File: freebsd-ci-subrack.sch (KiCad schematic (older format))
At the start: 1 part

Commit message: Add main parts
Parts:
- added C?: 100n, symbol Device:C
- added C?: 10n, symbol Device:C
- added D?: RX, symbol Device:LED
- added D?: TX, symbol Device:LED
- added D?: TGT_PWR, symbol Device:LED
- added Q?: Q_PMOS_GDS, symbol Device:Q_PMOS_GDS
- added Q?: 2N7002, Package_TO_SOT_SMD:SOT-23, symbol Transistor_FET:2N7002
- added R?: R, symbol Device:R
- added R? (x5): 5K, symbol Device:R
- added R?: 100K, symbol Device:R
- added R? (x2): 10K, symbol Device:R
- added TP?: SDA, symbol Connector:TestPoint
- added TP?: SCL, symbol Connector:TestPoint
- added U?: MCP2221A, symbol Subrack:MCP2221A
- added U?: INA219BxD, Package_SO:SOIC-8_3.9x4.9mm_P1.27mm, symbol Analog_ADC:INA219BxD
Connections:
- net labels added: +3V3, +5V_SW, +5V_TGT, PWRON, SCL, SDA
- wire segments 17 -> 81
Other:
- note added: "Backplane Connector"
- note added: "USB Interface"
- moved on the sheet: J?

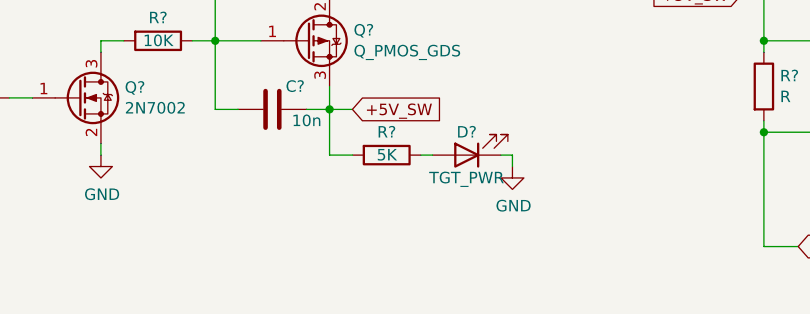
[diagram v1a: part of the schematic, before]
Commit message: Add reference to ON Semi load switch app note
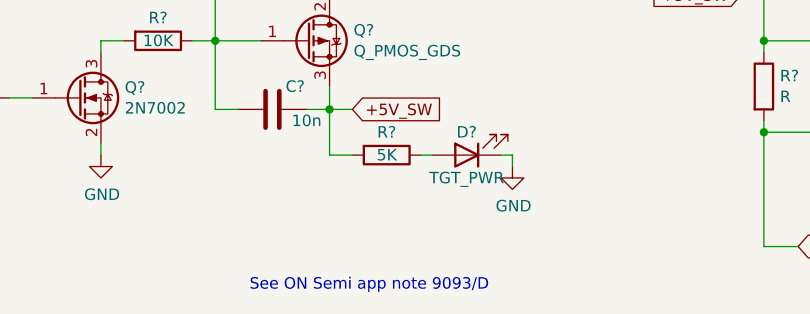
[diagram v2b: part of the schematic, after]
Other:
- note added: "See ON Semi app note 9093/D"
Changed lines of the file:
@@
 	4850 5800 5000 5800
 Connection ~ 4850 5300
+Text Notes 2600 6000 0    50   ~ 0
+See ON Semi app note 9093/D
 $EndSCHEMATC

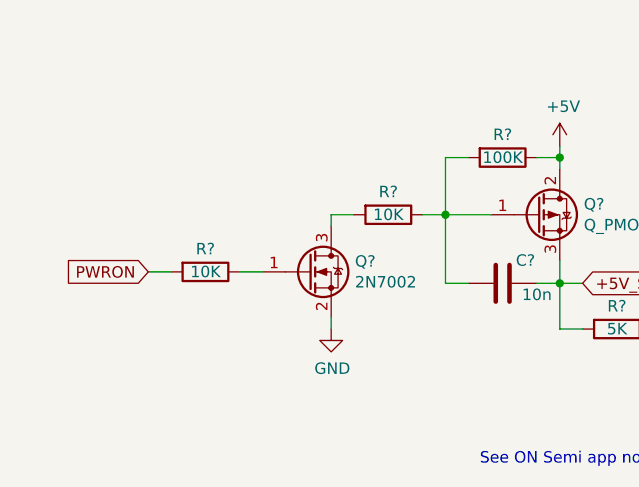
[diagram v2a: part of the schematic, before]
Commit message: Use an inverter instead of 2N7002
Allow us to drive the gate high, turning the PFET off more
quickly.
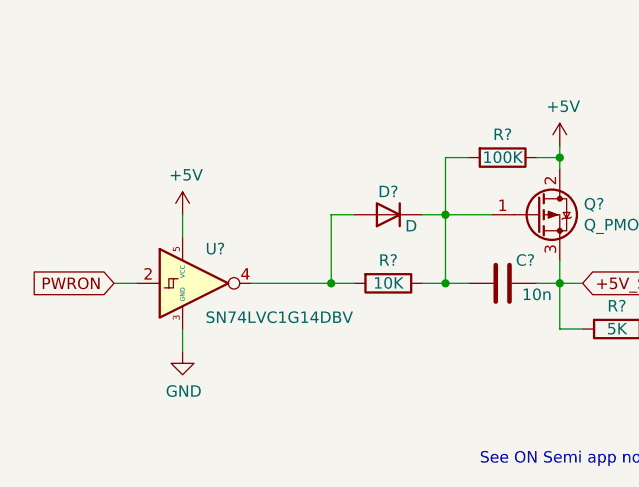
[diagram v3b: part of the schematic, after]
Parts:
- removed Q?: 2N7002, Package_TO_SOT_SMD:SOT-23, symbol Transistor_FET:2N7002
- removed R?: 10K, symbol Device:R
- added D?: D, symbol Device:D
- added U?: SN74LVC1G14DBV, Package_TO_SOT_SMD:SOT-23-5, symbol 74xGxx:SN74LVC1G14DBV
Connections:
- wire segments 81 -> 84
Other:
- moved on the sheet: R?
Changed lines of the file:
@@
 	2950 4600 2950 4650
-$Comp
-L Transistor_FET:2N7002 Q?
-U 1 1 609C94BD
-P 1850 5150
-F 0 "Q?" H 2054 5196 50  0000 L CNN
-F 1 "2N7002" H 2054 5105 50  0000 L CNN
-F 2 "Package_TO_SOT_SMD:SOT-23" H 2050 5075 50  0001 L CIN
-F 3 "https://www.onsemi.com/pub/Collateral/NDS7002A-D.PDF" H 1850 5150 50  0001 L CNN
-	1    1850 5150
-	1    0    0    -1
-$EndComp
-$Comp
-L power:GND #PWR?
-U 1 1 609CBBCB
-P 1950 5400
-F 0 "#PWR?" H 1950 5150 50  0001 C CNN
-F 1 "GND" H 1955 5227 50  0000 C CNN
-F 2 "" H 1950 5400 50  0001 C CNN
-F 3 "" H 1950 5400 50  0001 C CNN
-	1    1950 5400
-	1    0    0    -1
-$EndComp
 $Comp
 L Device:C C?
@@
 L Device:R R?
 U 1 1 609D742E
-P 2200 4900
-F 0 "R?" V 2100 4900 50  0000 C CNN
-F 1 "10K" V 2200 4900 50  0000 C CNN
-F 2 "" V 2130 4900 50  0001 C CNN
-F 3 "~" H 2200 4900 50  0001 C CNN
-	1    2200 4900
-	0    1    1    0
-$EndComp
-Wire Wire Line
-	2050 4900 1950 4900
-Wire Wire Line
-	1950 4900 1950 4950
-Wire Wire Line
-	1950 5350 1950 5400
+P 2200 5200
+F 0 "R?" V 2100 5200 50  0000 C CNN
+F 1 "10K" V 2200 5200 50  0000 C CNN
+F 2 "" V 2130 5200 50  0001 C CNN
+F 3 "~" H 2200 5200 50  0001 C CNN
+	1    2200 5200
+	0    1    1    0
+$EndComp
 $Comp
 L Device:LED D?
@@
 	9250 1050 9250 1150
 Connection ~ 9250 1150
-Text GLabel 1150 5150 0    50   Input ~ 0
+Text GLabel 1000 5200 0    50   Input ~ 0
 PWRON
-$Comp
-L Device:R R?
-U 1 1 60A711D5
-P 1400 5150
-F 0 "R?" V 1300 5150 50  0000 C CNN
-F 1 "10K" V 1400 5150 50  0000 C CNN
-F 2 "" V 1330 5150 50  0001 C CNN
-F 3 "~" H 1400 5150 50  0001 C CNN
-	1    1400 5150
-	0    1    1    0
-$EndComp
-Wire Wire Line
-	1550 5150 1650 5150
-Wire Wire Line
-	1150 5150 1250 5150
 Text GLabel 4750 4700 0    50   Input ~ 0
 +5V_SW
@@
 Text Notes 2600 6000 0    50   ~ 0
 See ON Semi app note 9093/D
+$Comp
+L 74xGxx:SN74LVC1G14DBV U?
+U 1 1 60A853C9
+P 1300 5200
+F 0 "U?" H 1400 5350 50  0000 L CNN
+F 1 "SN74LVC1G14DBV" H 1400 5050 50  0000 L CNN
+F 2 "Package_TO_SOT_SMD:SOT-23-5" H 1300 4950 50  0001 C CNN
+F 3 "http://www.ti.com/lit/ds/symlink/sn74lvc1g14.pdf" H 1300 5200 50  0001 C CNN
+	1    1300 5200
+	1    0    0    -1
+$EndComp
+Wire Wire Line
+	1000 5200 1100 5200
+$Comp
+L Device:D D?
+U 1 1 60A911C4
+P 2200 4900
+F 0 "D?" H 2200 4800 50  0000 C CNN
+F 1 "D" H 2100 4950 50  0000 C CNN
+F 2 "" H 2200 4900 50  0001 C CNN
+F 3 "~" H 2200 4900 50  0001 C CNN
+	1    2200 4900
+	-1   0    0    1
+$EndComp
+Wire Wire Line
+	2350 5200 2450 5200
+Connection ~ 2450 5200
+Wire Wire Line
+	2050 5200 1950 5200
+Wire Wire Line
+	1950 5200 1950 4900
+Wire Wire Line
+	1950 4900 2050 4900
+Wire Wire Line
+	1600 5200 1950 5200
+Connection ~ 1950 5200
+$Comp
+L power:+5V #PWR?
+U 1 1 60AA2B40
+P 1300 4900
+F 0 "#PWR?" H 1300 4750 50  0001 C CNN
+F 1 "+5V" H 1315 5073 50  0000 C CNN
+F 2 "" H 1300 4900 50  0001 C CNN
+F 3 "" H 1300 4900 50  0001 C CNN
+	1    1300 4900
+	1    0    0    -1
+$EndComp
+Wire Wire Line
+	1300 5000 1300 4900
+$Comp
+L power:GND #PWR?
+U 1 1 60AA5425
+P 1300 5500
+F 0 "#PWR?" H 1300 5250 50  0001 C CNN
+F 1 "GND" H 1305 5327 50  0000 C CNN
+F 2 "" H 1300 5500 50  0001 C CNN
+F 3 "" H 1300 5500 50  0001 C CNN
+	1    1300 5500
+	1    0    0    -1
+$EndComp
+Wire Wire Line
+	1300 5500 1300 5400
 $EndSCHEMATC

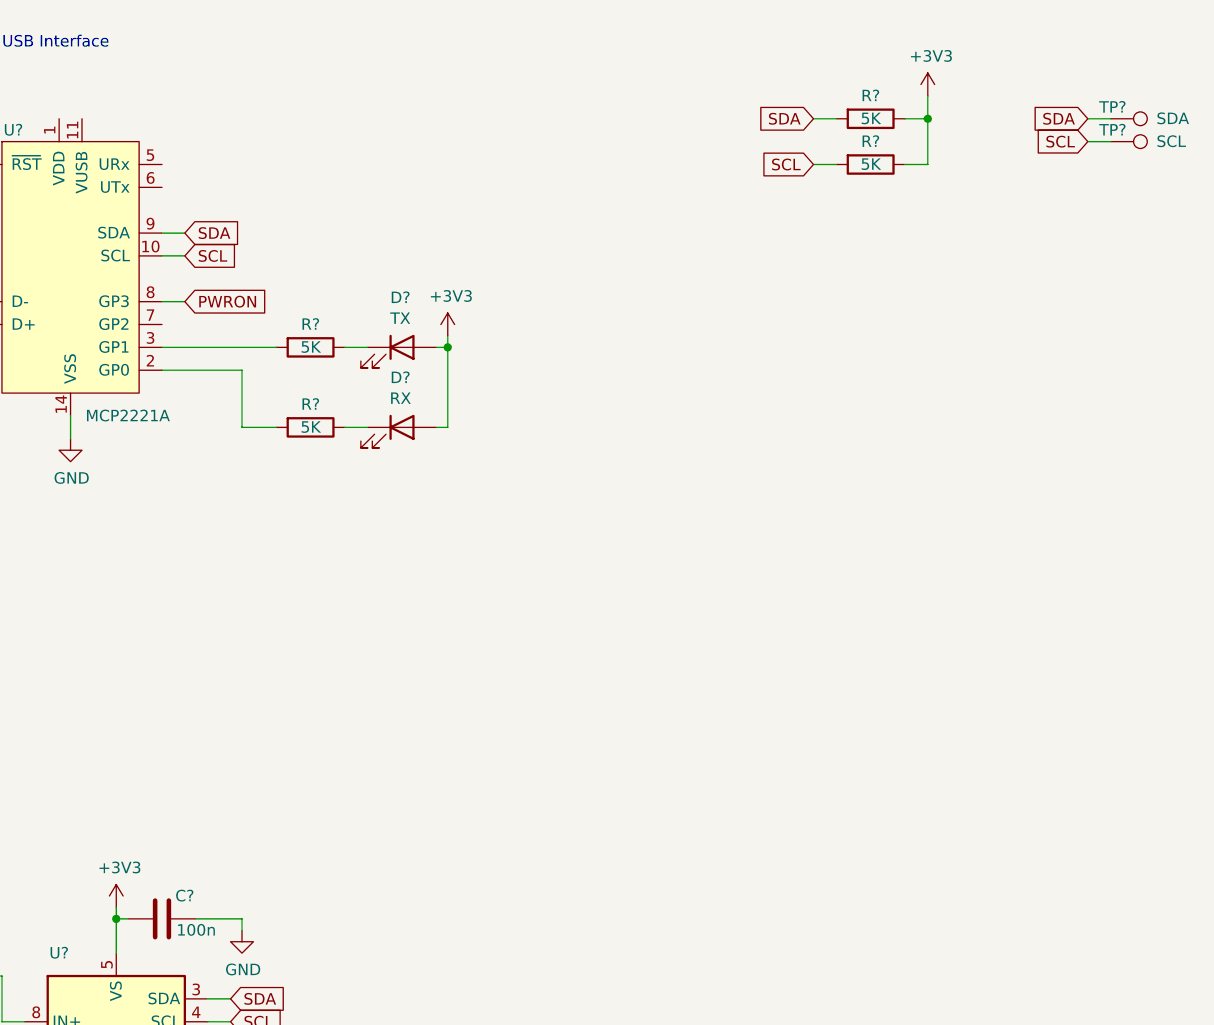
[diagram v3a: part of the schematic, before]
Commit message: Add a buffer for TX to target
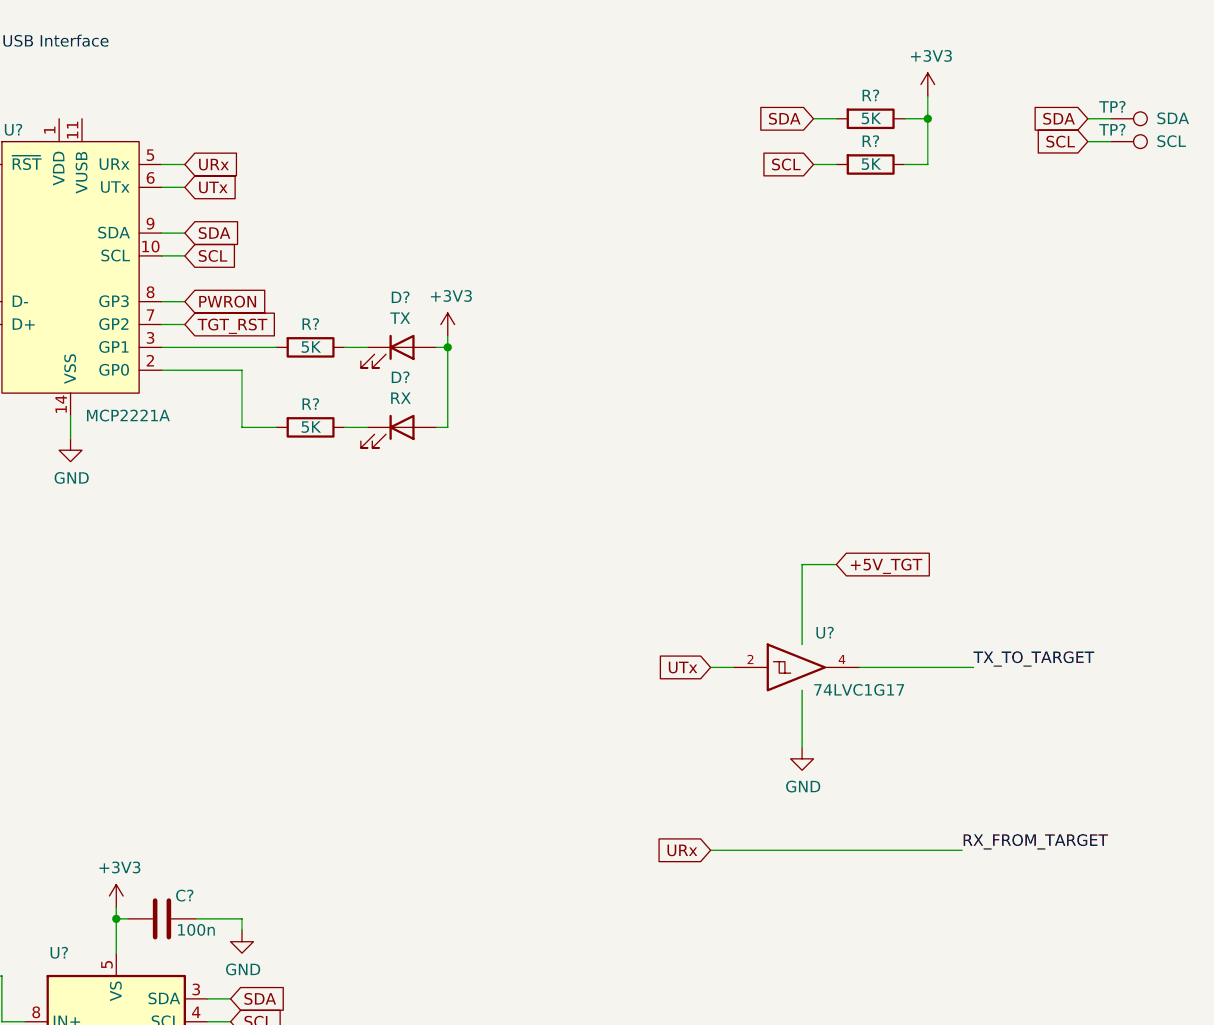
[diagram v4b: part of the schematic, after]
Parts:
- added U?: 74LVC1G17, symbol 74xGxx:74LVC1G17
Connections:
- net labels added: RX_FROM_TARGET, TGT_RST, TX_TO_TARGET, URx, UTx
- wire segments 84 -> 93
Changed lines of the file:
@@
 Wire Wire Line
 	1300 5500 1300 5400
+$Comp
+L 74xGxx:74LVC1G17 U?
+U 1 1 60AADB57
+P 8700 3550
+F 0 "U?" H 8800 3700 50  0000 C CNN
+F 1 "74LVC1G17" H 8950 3450 50  0000 C CNN
+F 2 "" H 8700 3550 50  0001 C CNN
+F 3 "http://www.ti.com/lit/sg/scyt129e/scyt129e.pdf" H 8700 3550 50  0001 C CNN
+	1    8700 3550
+	1    0    0    -1
+$EndComp
+Text GLabel 8850 3100 2    50   Input ~ 0
++5V_TGT
+Wire Wire Line
+	8700 3450 8700 3100
+Wire Wire Line
+	8700 3100 8850 3100
+$Comp
+L power:GND #PWR?
+U 1 1 60AB1679
+P 8700 3900
+F 0 "#PWR?" H 8700 3650 50  0001 C CNN
+F 1 "GND" H 8705 3727 50  0000 C CNN
+F 2 "" H 8700 3900 50  0001 C CNN
+F 3 "" H 8700 3900 50  0001 C CNN
+	1    8700 3900
+	1    0    0    -1
+$EndComp
+Wire Wire Line
+	8700 3650 8700 3900
+Text GLabel 6000 1350 2    50   Input ~ 0
+URx
+Text GLabel 6000 1450 2    50   Input ~ 0
+UTx
+Wire Wire Line
+	5900 1450 6000 1450
+Wire Wire Line
+	5900 1350 6000 1350
+Text GLabel 8300 3550 0    50   Input ~ 0
+UTx
+Wire Wire Line
+	8300 3550 8400 3550
+Text Label 9450 3550 0    50   ~ 0
+TX_TO_TARGET
+Wire Wire Line
+	8950 3550 9450 3550
+Text GLabel 8300 4350 0    50   Input ~ 0
+URx
+Text Label 9400 4350 0    50   ~ 0
+RX_FROM_TARGET
+Wire Wire Line
+	8300 4350 9400 4350
+Text GLabel 6000 2050 2    50   Input ~ 0
+TGT_RST
+Wire Wire Line
+	5900 2050 6000 2050
 $EndSCHEMATC

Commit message: Change 12V to NC - we're not using it on this board
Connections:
- net labels removed: +12V
- wire segments 93 -> 89
- no-connect marks 0 -> 2
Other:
- note added: "12V"
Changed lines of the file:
@@
 $EndComp
-$Comp
-L power:+12V #PWR?
-U 1 1 60985629
-P 1300 1350
-F 0 "#PWR?" H 1300 1200 50  0001 C CNN
-F 1 "+12V" H 1315 1523 50  0000 C CNN
-F 2 "" H 1300 1350 50  0001 C CNN
-F 3 "" H 1300 1350 50  0001 C CNN
-	1    1300 1350
-	1    0    0    -1
-$EndComp
-Wire Wire Line
-	1350 1400 1300 1400
-Wire Wire Line
-	1300 1400 1300 1350
-$Comp
-L power:+12V #PWR?
-U 1 1 60986720
-P 1900 1350
-F 0 "#PWR?" H 1900 1200 50  0001 C CNN
-F 1 "+12V" H 1915 1523 50  0000 C CNN
-F 2 "" H 1900 1350 50  0001 C CNN
-F 3 "" H 1900 1350 50  0001 C CNN
-	1    1900 1350
-	1    0    0    -1
-$EndComp
-Wire Wire Line
-	1850 1400 1900 1400
-Wire Wire Line
-	1900 1400 1900 1350
 $Comp
 L power:+5V #PWR?
@@
 Wire Wire Line
 	5900 2050 6000 2050
+NoConn ~ 1350 1400
+NoConn ~ 1850 1400
+Text Notes 1900 1400 0    50   ~ 0
+12V
+Text Notes 1300 1400 2    50   ~ 0
+12V
 $EndSCHEMATC
